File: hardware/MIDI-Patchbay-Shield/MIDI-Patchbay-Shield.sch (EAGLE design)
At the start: 82 parts, among them T1 BC817, T2 BC817, U1 VO2630SMD, U2 VO2630SMD

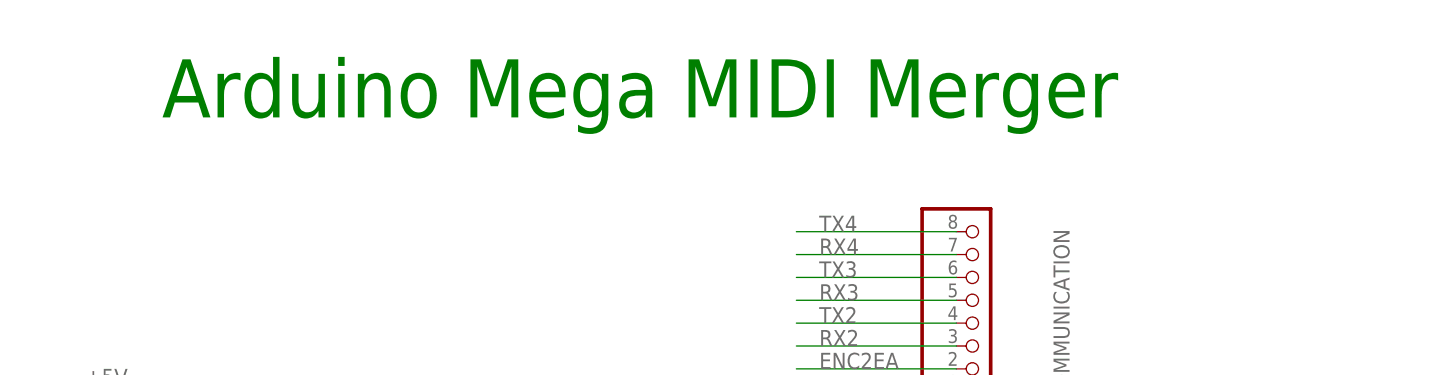
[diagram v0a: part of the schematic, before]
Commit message: Added images for boards and schematics
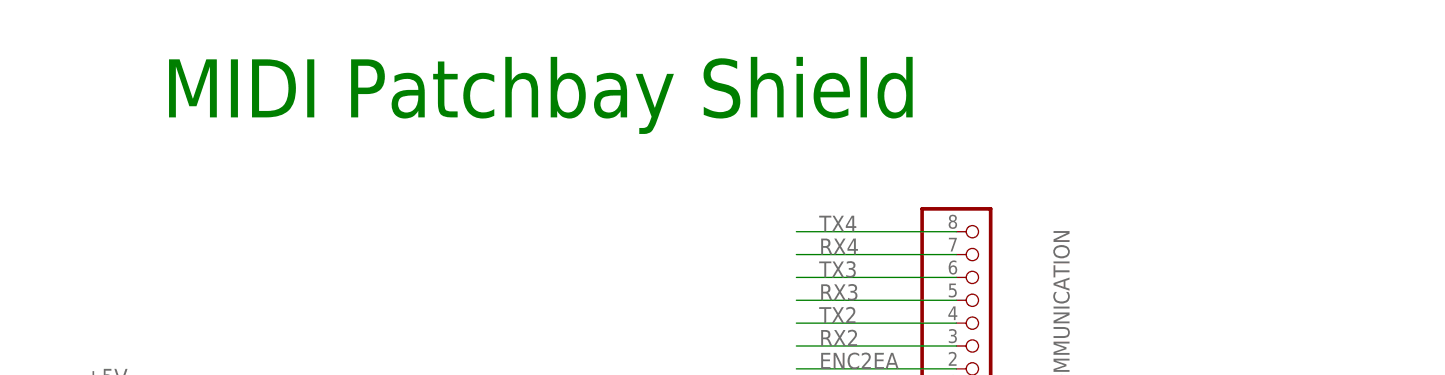
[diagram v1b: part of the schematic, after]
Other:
- note added: "MIDI Patchbay Shield"
- note removed: "Arduino Mega MIDI Merger"
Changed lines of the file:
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@@
 <text x="191.135" y="156.845" size="1.778" layer="91">12</text>
 <text x="191.135" y="159.385" size="1.778" layer="91">13</text>
-<text x="97.155" y="208.28" size="6.4516" layer="91">Arduino Mega MIDI Merger</text>
+<text x="97.155" y="208.28" size="6.4516" layer="91">MIDI Patchbay Shield</text>
 <text x="165.735" y="52.07" size="1.6764" layer="91">(SS)</text>
 <text x="165.735" y="49.53" size="1.6764" layer="91">(MOSI)</text>
